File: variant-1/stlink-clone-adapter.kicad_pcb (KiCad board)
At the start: 2 copper layers, 15 x 14.2 mm, 2 parts, among them J1 2X5_HDR, J2 ARM_10PIN

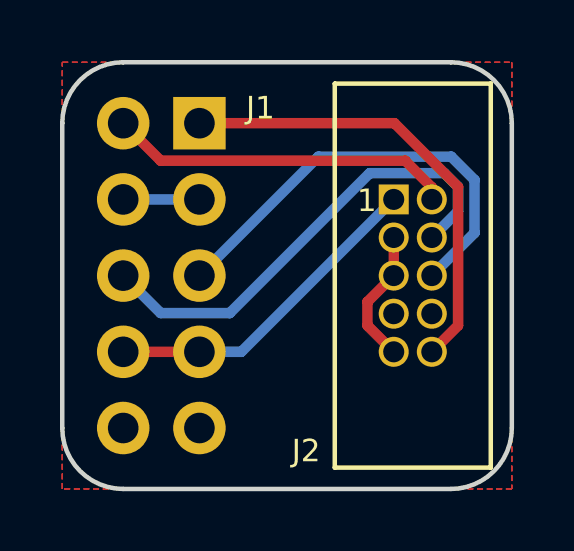
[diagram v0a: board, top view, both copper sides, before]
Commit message: pour bottom ground
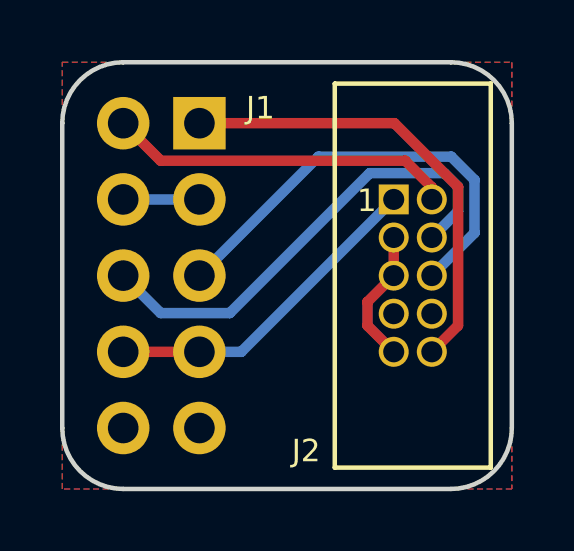
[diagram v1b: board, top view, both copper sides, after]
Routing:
- added copper zone on B.Cu, net /GND
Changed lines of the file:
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@@
-(kicad_pcb (version 20171130) (host pcbnew 5.1.8-db9833491~88~ubuntu20.04.1)
+(kicad_pcb (version 20171130) (host pcbnew 5.1.9-73d0e3b20d~88~ubuntu20.10.1)
   (general
     (thickness 1.6)
@@
   )
   (setup
-    (last_trace_width 0.35)
+    (last_trace_width 0.25)
     (user_trace_width 0.35)
     (trace_clearance 0.2)
@@
       (effects (font (size 0.75 0.75) (thickness 0.12)))
     )
+    (fp_line (start 2.6 -6.4) (end 2.6 6.4) (layer F.SilkS) (width 0.15))
+    (fp_line (start 2.6 6.4) (end -2.6 6.4) (layer F.SilkS) (width 0.15))
+    (fp_line (start -2.6 6.4) (end -2.6 -6.4) (layer F.SilkS) (width 0.15))
     (fp_line (start -2.6 -6.4) (end 2.6 -6.4) (layer F.SilkS) (width 0.15))
-    (fp_line (start -2.6 6.4) (end -2.6 -6.4) (layer F.SilkS) (width 0.15))
-    (fp_line (start 2.6 6.4) (end -2.6 6.4) (layer F.SilkS) (width 0.15))
-    (fp_line (start 2.6 -6.4) (end 2.6 6.4) (layer F.SilkS) (width 0.15))
     (fp_text user 1 (at -1.535 -2.5) (layer F.SilkS)
       (effects (font (size 0.75 0.75) (thickness 0.12)))
@@
     )
   )
-  (zone (net 3) (net_name /GND) (layer F.Cu) (hatch edge 0.508)
+  (zone (net 3) (net_name /GND) (layer B.Cu) (hatch edge 0.508)
     (connect_pads (clearance 0.35))
     (min_thickness 0.254)
